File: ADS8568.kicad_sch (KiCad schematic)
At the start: 44 parts, among them U1301 ADS8568

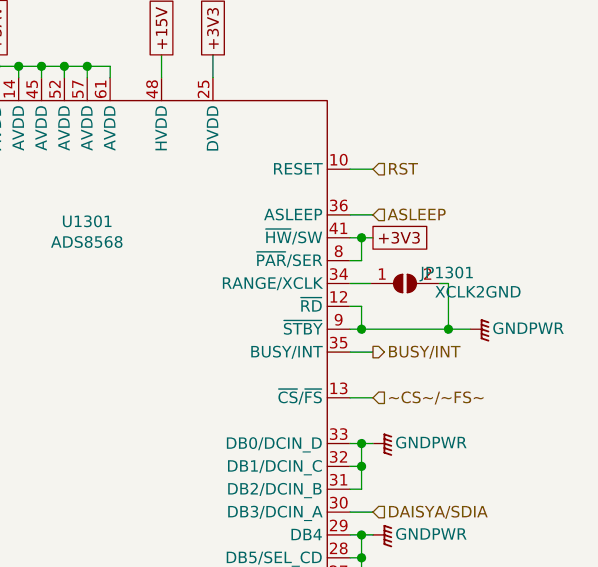
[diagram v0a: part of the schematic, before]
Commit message: FEAR-16 V2.2
PCB-Changes:
 - Added rudimentary "load-balancer" (not really a balancer, but should avoid the DC/DC from regulating against each other!)
 - Added optional GND-jumpers to the N/C pins of the shields
 - Modified amplification adjustment:
   -> Added a offset resistor in row to the trim-poti for amplification for finer amp-tuning
   -> Reduced trim-poti-value from 1Meg -> 50k (20x finer adjustment-range)
      Poti can in the range of:
      - 30k (min) for being able to reach the correct amplification
      - 50k (max) for having at least 20x finer tune-range and a bit of reserve, as 30k is pretty thight on tolerance

Misc.:
 - Added LICENSE.md
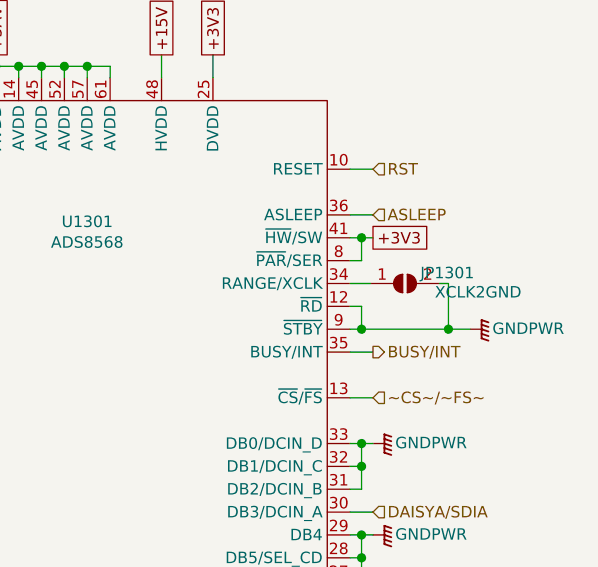
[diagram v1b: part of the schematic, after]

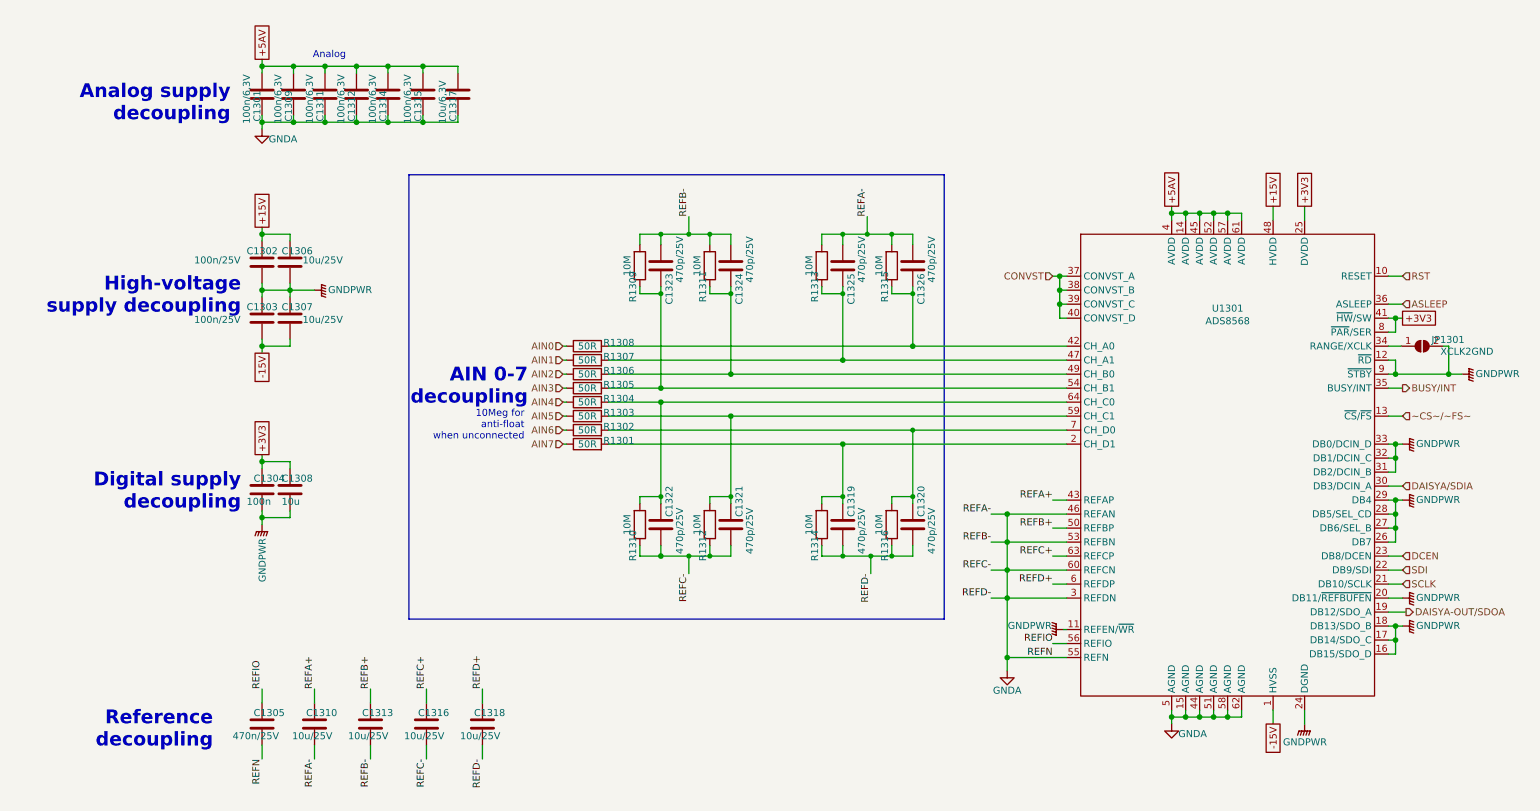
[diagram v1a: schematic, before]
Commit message: Fixed ADP2370 designator
ADP2370 has a bunch of fixed output voltages and an adjustable model.
We use the adjustable model, so we fixed the name matching with the correct model-name.
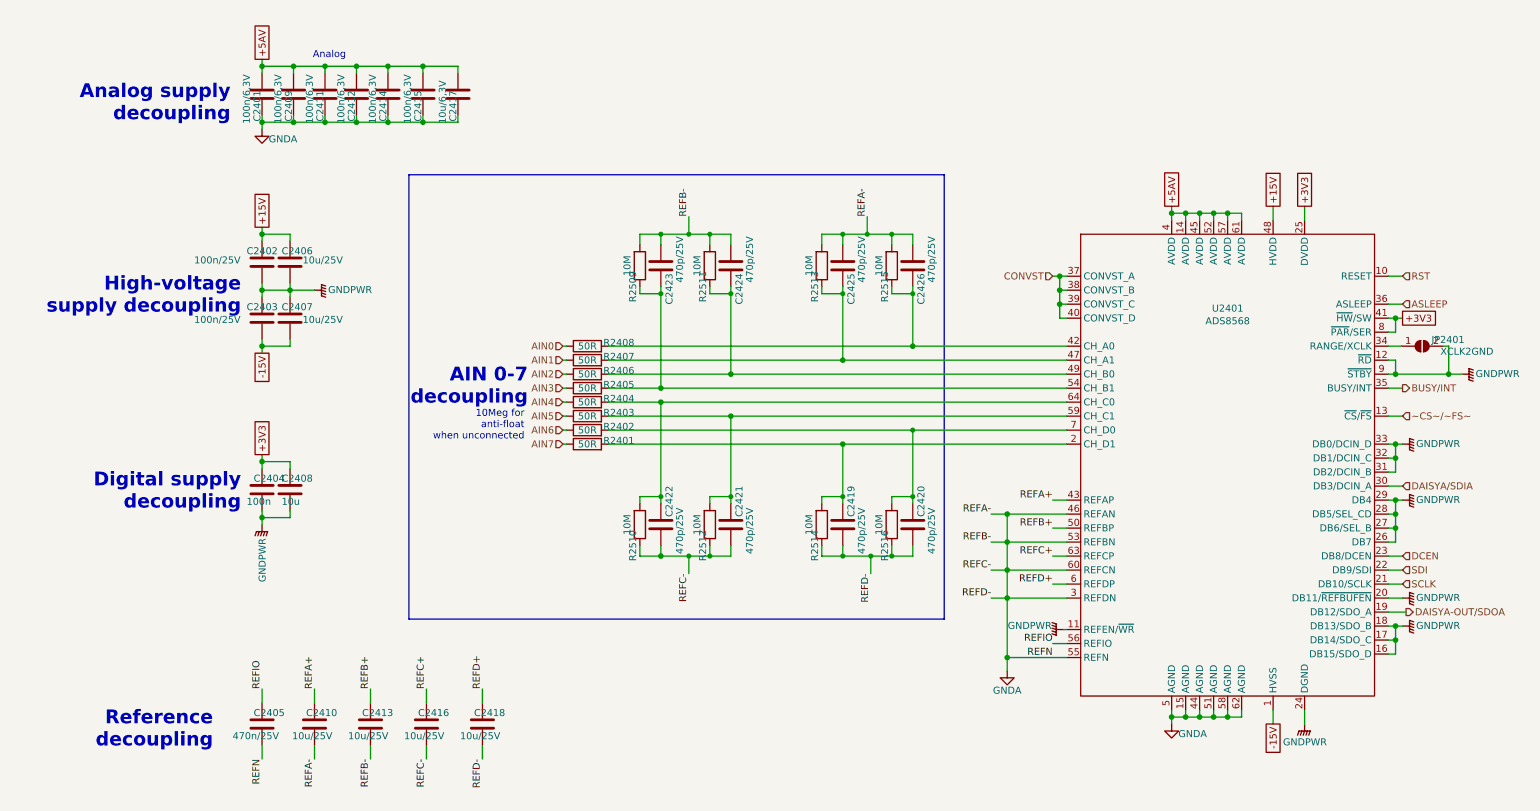
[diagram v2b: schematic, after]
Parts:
- renumbered C1301 to C2401, C1302 to C2402, C1303 to C2403, C1304 to C2404, C1305 to C2405, C1306 to C2406, C1307 to C2407, C1308 to C2408, C1309 to C2409, C1310 to C2410, C1311 to C2411, C1312 to C2412, C1313 to C2413, C1314 to C2414, C1315 to C2415, C1316 to C2416, C1317 to C2417, C1318 to C2418, C1319 to C2419, C1320 to C2420, C1321 to C2421, C1322 to C2422, C1323 to C2423, C1324 to C2424, C1325 to C2425, C1326 to C2426, JP1301 to JP2401, R1301 to R2401, R1302 to R2402, R1303 to R2403, R1304 to R2404, R1305 to R2405, R1306 to R2406, R1307 to R2407, R1308 to R2408, R1309 to R2509, R1310 to R2510, R1311 to R2511, R1312 to R2512, R1313 to R2513, R1314 to R2514, R1315 to R2515, R1316 to R2516, U1301 to U2401
